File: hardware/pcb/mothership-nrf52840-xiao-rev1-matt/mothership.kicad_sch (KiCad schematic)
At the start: 45 parts, among them J1 HRO TYPE-C-31-M-12, J10 CONN_BATT, J11 Screw_Terminal_ADB_VCC, J2 USB_FLEX_ADAPTER_SOLDER_PADS, J3 Screw_Terminal_ADB_SHIELD, J4 CONN_MATRIX_BOT_L, J5 CONN_MATRIX_BOT_R, J6 CONN_MATRIX_TOP_R, J7 CONN_MATRIX_TOP_L, J8 SPI, J9 EC11, Q1 AO3401A, Q2 FDC6305N, SW1 SW_SPDT_321, SW2 SW_SPST, U1 NCP361SN, U2 XIAO_nRF52840, U3 MCP23017x-x-SS, U4 MCP23017x-x-SS, U5 DT1452-02SO, U6 HY2115-LB9D

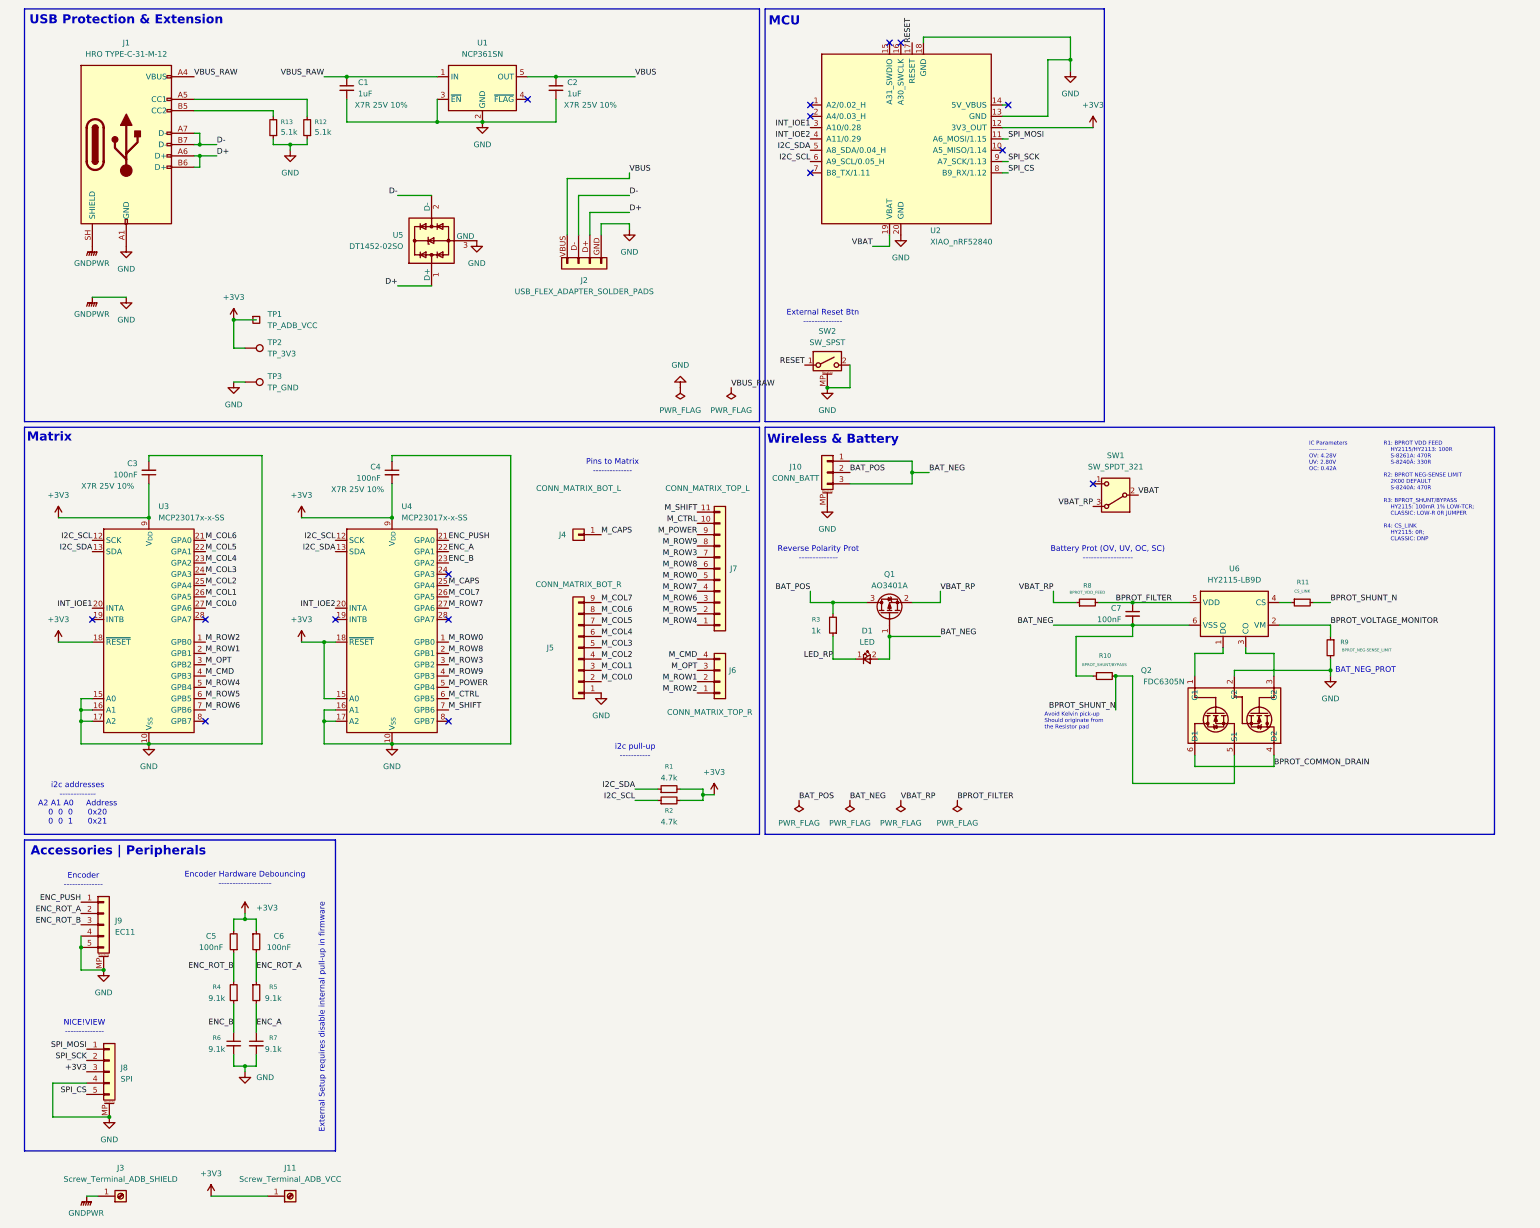
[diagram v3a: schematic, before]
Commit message: sch: fixing symbol & assigned footprints not matched
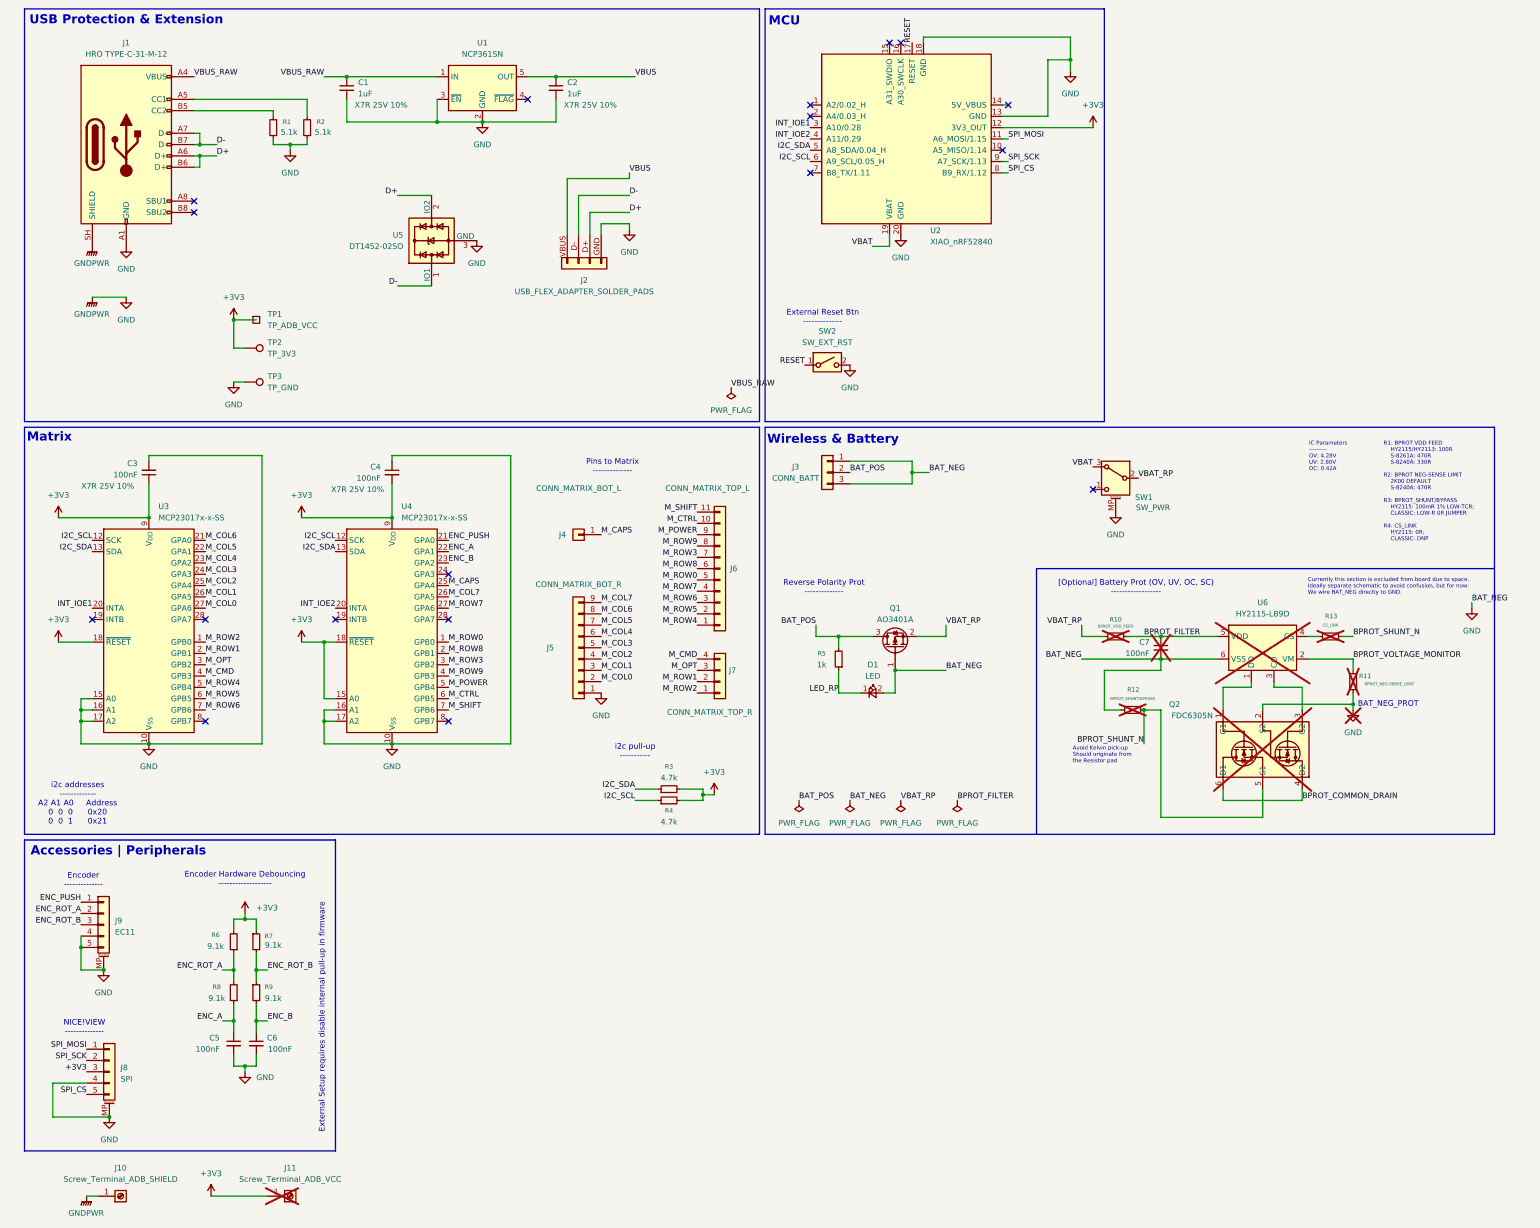
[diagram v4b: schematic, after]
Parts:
- C7, J11, Q2: now not fitted
- D1: footprint (none) -> A9M0330:LED_0805_2012Metric_Pad1.15x1.40mm_HandSolder
- J1: symbol A9M0330:USB_C_Receptacle_USB2.0_14P -> A9M0330:USB_C_Receptacle_USB2.0_16P
- J2: footprint (none) -> A9M0330:Conn_FFC-USB_Plug__4P_Flex_Adapter
- J3: renamed from J10; symbol A9M0330:Conn_01x03_MountingPin -> A9M0330:Conn_01x03
- J4: footprint (none) -> A9M0330:PinHeader_1x01_P2.54mm_Vertical
- J5: footprint (none) -> A9M0330:PinHeader_1x09_P2.54mm_Vertical
- J6: renamed from J7; footprint (none) -> A9M0330:PinHeader_1x11_P2.54mm_Vertical
- J7: renamed from J6; footprint (none) -> A9M0330:PinHeader_1x04_P2.54mm_Vertical
- J8, J9: footprint (none) -> A9M0330:Conn_JST__SH_SM05B-SRSS-TB_1x05-1MP_P1.00mm_Horizontal_HandSolder__Mounting_AnchorVias_Compat
- R10: renamed from R8; now not fitted
- R11: renamed from R9; now not fitted
- R12: renamed from R10; now not fitted
- R13: renamed from R11; now not fitted
- SW1: value SW_SPDT_321 -> SW_PWR; footprint A9M0330:SW_SPDT_SMD__Slide_321_Shouhan_MINI_MSK12C02__Mounting_AnchorVias -> A9M0330:SW_SPDT_SMD__Slide_321_Shouhan_MINI_MSK12C02_HandSolder__Mounting_AnchorVias; symbol A9M0330:SW_SPDT_321 -> A9M0330:SW_SPDT_321_MountingPin
- SW2: value SW_SPST -> SW_EXT_RST; footprint A9M0330:SW_SPDT_SMD__Slide_321_Shouhan_MINI_MSK12C02__Mounting_AnchorVias -> A9M0330:SW_Push_SMD__SPST_NO_Alps_SKRK; symbol A9M0330:SW_SPST_MountingPin -> A9M0330:SW_SPST
- TP1: footprint (none) -> A9M0330:TestPoint_Pad_2.5x2.5mm
- TP2: footprint (none) -> A9M0330:TestPoint_THTPad_D2.0mm_Drill1.0mm
- TP3: footprint (none) -> A9M0330:TestPoint_THTPad_2.0x2.0mm_Drill1.0mm
- U2: footprint (none) -> A9M0330:MCU_Module_nRF52840__XIAO_SMD_NoNFC_BottomPadCutoutTHT
- U6: footprint Package_TO_SOT_SMD:SOT-23-6 -> A9M0330:TO_SOT_SMD__SOT-23-6_MP006-A; now not fitted
- renumbered C6 to C5, C5 to C6, J3 to J10, R13 to R1, R12 to R2, R1 to R3, R2 to R4, R3 to R5, R7 to R6, R6 to R7, R4 to R8, R5 to R9
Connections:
- net BAT_NEG is gone; now on net GND: C7.2, D1.2 (A), J3.1 (Pin_1), J3.3 (Pin_3), Q1.1 (G), R12.1, U6.6 (VSS)
- net D+: now also U5.2 (IO2); no longer U5.1 (D+)
- net D-: now also U5.1 (IO1); no longer U5.2 (D-)
- net ENC_A: now also C5.1, R9.1; no longer C6.1, R8.2
- net ENC_B: now also C6.1, R8.2; no longer C5.1, R9.1
- net ENC_ROT_A: now also R6.1, R9.2; no longer R7.2, R8.1
- net ENC_ROT_B: now also R7.2, R8.1; no longer R6.1, R9.2
- net GND: now also SW1.MP (MountPin); no longer J3.MP (MountPin), SW2.MP (MountPin)
- net VBAT: now also SW1.3 (A); no longer SW1.2 (B)
- net VBAT_RP: now also SW1.2 (B); no longer SW1.3 (A)
- no-connect marks 16 -> 18
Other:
- note added: "Currently this section is excluded from board due to space. Ideally separate schematic to avoid confusion, but for now: We wire BAT_NEG directly to GND."
- note added: "[Optional] Battery Prot (OV, UV, OC, SC) ------------------"
- note removed: "Battery Prot (OV, UV, OC, SC) ------------------"
- moved on the sheet: D1, Q1, R5

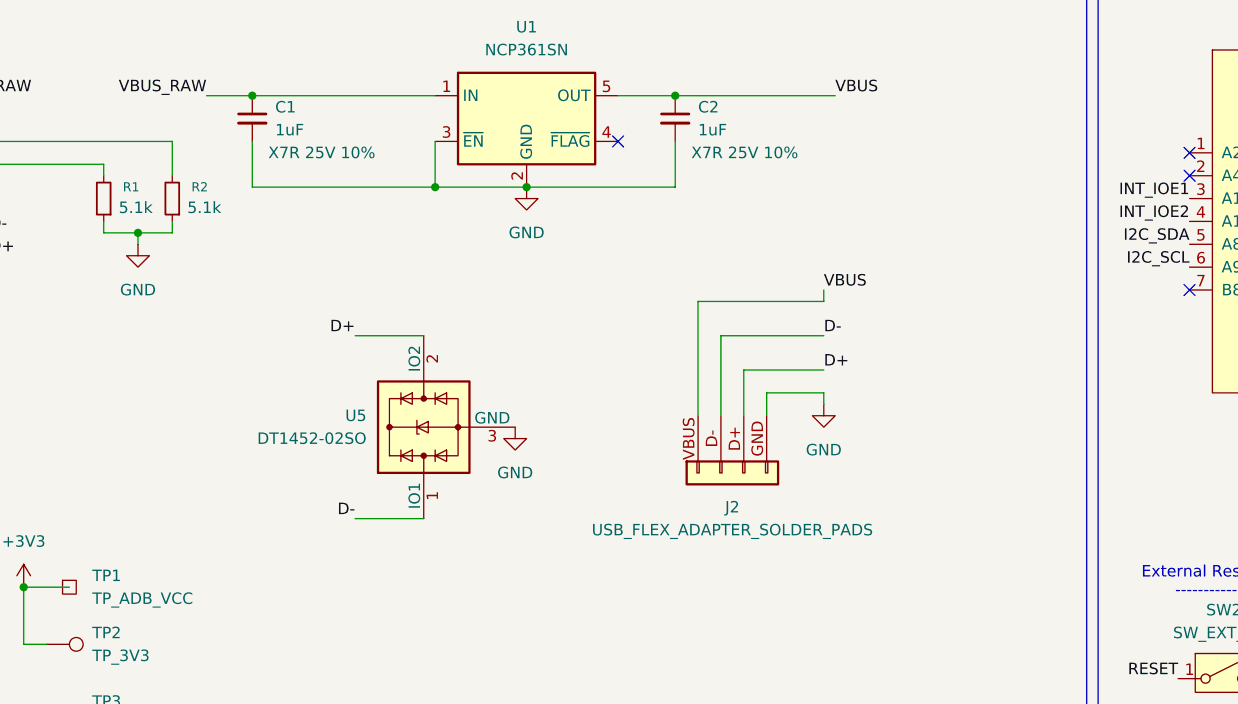
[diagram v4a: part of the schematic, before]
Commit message: sch: add another flex pad on top for usb-c cable
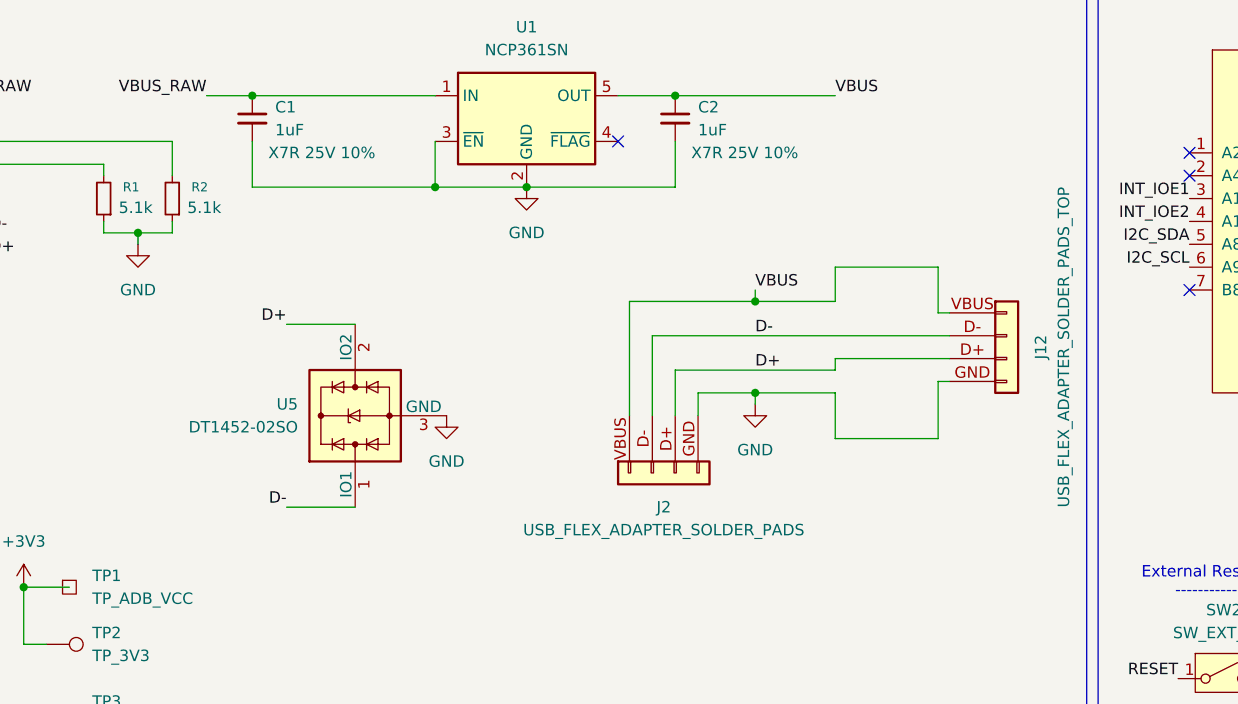
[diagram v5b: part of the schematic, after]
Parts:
- added J12: USB_FLEX_ADAPTER_SOLDER_PADS_TOP, A9M0330:Conn_FFC-USB_Plug__4P_Flex_Adapter, symbol A9M0330:Conn_01x04_USB_FFC
- J1: footprint A9M0330:USB_C_Receptacle__16P_HRO_TYPE-C-31-M-12_HandSolder -> A9M0330:USB_C_Receptacle__16P_HRO_TYPE-C-31-M-12_HandSolder_Universal
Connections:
- net D+: now also J12.D+
- net D-: now also J12.D-
- net GND: now also J12.GND
- net VBUS: now also J12.VBUS
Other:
- moved on the sheet: J2, U5

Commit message: sch: finalize the sch
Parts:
- added TP4: TP_ADB_VCC, A9M0330:TestPoint_Pad_2.5x2.5mm, symbol A9M0330:TestPoint_Square
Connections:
- net +3V3: now also TP4.1
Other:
- moved on the sheet: TP3
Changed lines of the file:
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@@
 	)
 	(junction
+		(at 59.69 88.9)
+		(diameter 0)
+		(color 0 0 0 0)
+	)
+	(junction
 		(at 132.08 27.94)
 		(diameter 0)
@@
 	(wire
 		(pts
+			(xy 59.69 88.9) (xy 59.69 95.25)
+		)
+		(stroke
+			(width 0)
+			(type default)
+		)
+	)
+	(wire
+		(pts
 			(xy 140.97 60.96) (xy 140.97 62.23)
 		)
@@
 	(wire
 		(pts
+			(xy 59.69 95.25) (xy 62.23 95.25)
+		)
+		(stroke
+			(width 0)
+			(type default)
+		)
+	)
+	(wire
+		(pts
 			(xy 59.69 236.22) (xy 59.69 240.03)
 		)
@@
 	(wire
 		(pts
-			(xy 59.69 96.52) (xy 62.23 96.52)
+			(xy 39.37 95.25) (xy 41.91 95.25)
 		)
 		(stroke
@@
 	(wire
 		(pts
-			(xy 59.69 88.9) (xy 62.23 88.9)
+			(xy 59.69 88.9) (xy 64.77 88.9)
 		)
 		(stroke
@@
 	)
 	(symbol
+		(lib_id "A9M0330:TestPoint")
+		(at 62.23 95.25 270)
+		(unit 1)
+		(body_style 1)
+		(exclude_from_sim no)
+		(in_bom yes)
+		(on_board yes)
+		(in_pos_files yes)
+		(dnp no)
+		(fields_autoplaced yes)
+		(property "Reference" "TP2"
+			(at 67.31 93.9799 90)
+			(show_name no)
+			(do_not_autoplace no)
+			(effects
+				(font
+					(size 1.27 1.27)
+				)
+				(justify left)
+			)
+		)
+		(property "Value" "TP_3V3"
+			(at 67.31 96.5199 90)
+			(show_name no)
+			(do_not_autoplace no)
+			(effects
+				(font
+					(size 1.27 1.27)
+				)
+				(justify left)
+			)
+		)
+		(property "Footprint" "A9M0330:TestPoint_THTPad_D2.0mm_Drill1.0mm"
+			(at 62.23 100.33 0)
+			(hide yes)
+			(show_name no)
+			(do_not_autoplace no)
+			(effects
+				(font
+					(size 1.27 1.27)
+				)
+			)
+		)
+		(property "Datasheet" ""
+			(at 62.23 100.33 0)
+			(hide yes)
+			(show_name no)
+			(do_not_autoplace no)
+			(effects
+				(font
+					(size 1.27 1.27)
+				)
+			)
+		)
+		(property "Description" "test point"
+			(at 62.23 95.25 0)
+			(hide yes)
+			(show_name no)
+			(do_not_autoplace no)
+			(effects
+				(font
+					(size 1.27 1.27)
+				)
+			)
+		)
+		(pin "1"
+		)
+		(instances
+			(project "mothership"
+				(path "/02dc08fe-8ec4-4078-b85a-ecd1690e4fdc"
+					(reference "TP2")
+					(unit 1)
+				)
+			)
+		)
+	)
+	(symbol
 		(lib_id "power:+3V3")
 		(at 74.93 127 0)
@@
 	)
 	(symbol
-		(lib_id "A9M0330:TestPoint")
-		(at 62.23 88.9 270)
-		(unit 1)
-		(body_style 1)
-		(exclude_from_sim no)
-		(in_bom yes)
-		(on_board yes)
-		(in_pos_files yes)
-		(dnp no)
-		(fields_autoplaced yes)
-		(property "Reference" "TP2"
-			(at 67.31 87.6299 90)
-			(show_name no)
-			(do_not_autoplace no)
-			(effects
-				(font
-					(size 1.27 1.27)
-				)
-				(justify left)
-			)
-		)
-		(property "Value" "TP_3V3"
-			(at 67.31 90.1699 90)
-			(show_name no)
-			(do_not_autoplace no)
-			(effects
-				(font
-					(size 1.27 1.27)
-				)
-				(justify left)
-			)
-		)
-		(property "Footprint" "A9M0330:TestPoint_THTPad_D2.0mm_Drill1.0mm"
-			(at 62.23 93.98 0)
-			(hide yes)
-			(show_name no)
-			(do_not_autoplace no)
-			(effects
-				(font
-					(size 1.27 1.27)
-				)
-			)
-		)
-		(property "Datasheet" ""
-			(at 62.23 93.98 0)
-			(hide yes)
-			(show_name no)
-			(do_not_autoplace no)
-			(effects
-				(font
-					(size 1.27 1.27)
-				)
-			)
-		)
-		(property "Description" "test point"
-			(at 62.23 88.9 0)
-			(hide yes)
-			(show_name no)
-			(do_not_autoplace no)
-			(effects
-				(font
-					(size 1.27 1.27)
-				)
-			)
-		)
-		(pin "1"
-		)
-		(instances
-			(project "mothership"
-				(path "/02dc08fe-8ec4-4078-b85a-ecd1690e4fdc"
-					(reference "TP2")
-					(unit 1)
-				)
-			)
-		)
-	)
-	(symbol
 		(lib_id "power:GND")
 		(at 337.82 147.32 0)
@@
 	(symbol
 		(lib_id "power:GND")
-		(at 59.69 96.52 0)
+		(at 39.37 95.25 0)
 		(unit 1)
 		(body_style 1)
@@
 		(fields_autoplaced yes)
 		(property "Reference" "#PWR011"
-			(at 59.69 102.87 0)
+			(at 39.37 101.6 0)
 			(hide yes)
 			(show_name no)
@@
 		)
 		(property "Value" "GND"
-			(at 59.69 101.6 0)
+			(at 39.37 100.33 0)
 			(show_name no)
 			(do_not_autoplace no)
@@
 		)
 		(property "Footprint" ""
-			(at 59.69 96.52 0)
+			(at 39.37 95.25 0)
 			(hide yes)
 			(show_name no)
@@
 		)
 		(property "Datasheet" ""
-			(at 59.69 96.52 0)
+			(at 39.37 95.25 0)
 			(hide yes)
 			(show_name no)
@@
 		)
 		(property "Description" "Power symbol creates a global label with name \"GND\" , ground"
-			(at 59.69 96.52 0)
+			(at 39.37 95.25 0)
 			(hide yes)
 			(show_name no)
@@
 	(symbol
 		(lib_id "A9M0330:TestPoint")
-		(at 62.23 96.52 270)
+		(at 41.91 95.25 270)
 		(unit 1)
 		(body_style 1)
@@
 		(fields_autoplaced yes)
 		(property "Reference" "TP3"
-			(at 67.31 95.2499 90)
+			(at 46.99 93.9799 90)
 			(show_name no)
 			(do_not_autoplace no)
@@
 		)
 		(property "Value" "TP_GND"
-			(at 67.31 97.7899 90)
+			(at 46.99 96.5199 90)
 			(show_name no)
 			(do_not_autoplace no)
@@
 		)
 		(property "Footprint" "A9M0330:TestPoint_THTPad_2.0x2.0mm_Drill1.0mm"
-			(at 62.23 101.6 0)
+			(at 41.91 100.33 0)
 			(hide yes)
 			(show_name no)
@@
 		)
 		(property "Datasheet" ""
-			(at 62.23 101.6 0)
+			(at 41.91 100.33 0)
 			(hide yes)
 			(show_name no)
@@
 		)
 		(property "Description" "test point"
-			(at 62.23 96.52 0)
+			(at 41.91 95.25 0)
 			(hide yes)
 			(show_name no)
@@
 					(unit 1)
 				)
+			)
+		)
+	)
+	(symbol
+		(lib_id "A9M0330:TestPoint_Square")
+		(at 64.77 88.9 0)
+		(unit 1)
+		(body_style 1)
+		(exclude_from_sim no)
+		(in_bom yes)
+		(on_board yes)
+		(in_pos_files yes)
+		(dnp no)
+		(property "Reference" "TP4"
+			(at 67.31 87.6299 0)
+			(show_name no)
+			(do_not_autoplace no)
+			(effects
+				(font
+					(size 1.27 1.27)
+				)
+				(justify left)
+			)
+		)
+		(property "Value" "TP_ADB_VCC"
+			(at 67.31 90.17 0)
+			(show_name no)
+			(do_not_autoplace no)
+			(effects
+				(font
+					(size 1.27 1.27)
+				)
+				(justify left)
+			)
+		)
+		(property "Footprint" "A9M0330:TestPoint_Pad_2.5x2.5mm"
+			(at 69.85 88.9 0)
+			(hide yes)
+			(show_name no)
+			(do_not_autoplace no)
+			(effects
+				(font
+					(size 1.27 1.27)
+				)
+			)
+		)
+		(property "Datasheet" "~"
+			(at 69.85 88.9 0)
+			(hide yes)
+			(show_name no)
+			(do_not_autoplace no)
+			(effects
+				(font
+					(size 1.27 1.27)
+				)
+			)
+		)
+		(property "Description" "test point"
+			(at 64.77 88.9 0)
+			(hide yes)
+			(show_name no)
+			(do_not_autoplace no)
+			(effects
+				(font
+					(size 1.27 1.27)
+				)
+			)
+		)
+		(pin "1"
+		)
+		(instances
+			(project "mothership"
+				(path "/02dc08fe-8ec4-4078-b85a-ecd1690e4fdc"
+					(reference "TP4")
+					(unit 1)
+				)
